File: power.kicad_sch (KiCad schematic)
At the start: 37 parts, among them J1 JST_PH_2.0mm_1x02, Q1 DMG2305UX-13, Q2 FS8205A, Q3 DMG2305UX-13, Q4 AO3400A, Q5 AO3400A, U1 DW01A, U2 LP5907MFX-3.3/NOPB, U3 TP4056, U4 LP5907MFX-3.3/NOPB, U5 SD6210A

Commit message: New components added, schematic being completed
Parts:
- added C38, C42, C54: 10u, sldrnrd:C_1206, symbol sldrnrd:Capacitor/C1206_10u
- added C40, C44: 100n, sldrnrd:C_0603, symbol sldrnrd:Capacitor/C0603_100n
- added C45: 1u, sldrnrd:C_0805, symbol sldrnrd:Capacitor/C0805_1u
- added R33: 68k, sldrnrd:R_0603, symbol sldrnrd:Resistor/R0603_68k
- added R35: 180k, sldrnrd:R_0603, symbol sldrnrd:Resistor/R0603_180k
- added U17: LM27761DSGR, sldrnrd:WSON-8-2x2-EP, symbol sldrnrd:Power/ChargePump/LM27761DSGR
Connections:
- net 5V0: now also C38.1, C40.1, U17.1 (VIN), U17.6 (EN)
- net GND: now also C38.2, C40.2, C42.2, C44.2, C54.2, R33.2, U17.2 (GND), U17.9 (EP)
- new net: R33.1, R35.2, U17.5 (VFB)
- new net: C54.1, U17.3 (CPOUT)
- new net: C45.1, U17.8 (C1+)
- new net: C45.2, U17.7 (C1-)
- new net -4V5: C42.1, C44.1, R35.1, U17.4 (VOUT)
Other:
- note added: "LM27761 Voltage Inverter"
- moved on the sheet: C1, C10, C11, C12, C14, C15, C2, C4, C6, C8, C9, Q3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

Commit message: Board layout without errors
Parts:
- renumbered C11 to C10, C7 to C11, C14 to C13, C15 to C14, C45 to C15, C54 to C16, C38 to C17, C40 to C18, C13 to C19, C42 to C20, C44 to C21, C4 to C3, C6 to C4, C3 to C5, C8 to C6, C9 to C7, C10 to C8, C5 to C9, Q3 to Q2, Q2 to Q3, R8 to R10, R9 to R11, R35 to R8, R33 to R9, U2 to U1, U1 to U2, U4 to U3, U3 to U4, U17 to U6

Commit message: Unavailable parts replaced, rotation issues fixed in library, except for U7
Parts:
- Q3: footprint sldrnrd:TSSOP-8 -> sldrnrd:SOT-23-6; symbol sldrnrd:Transistor/MosfetN/FS8205A -> sldrnrd:Transistor/MosfetN/FS8205A_TechPublic; LCSC C14212 -> C2830320; Manufacturer Fortune Semicon -> TECH PUBLIC
- R2: value 2k -> 1k; symbol sldrnrd:Resistor/R0603_2k -> sldrnrd:Resistor/R0603_1k; LCSC C22975 -> C21190; MPN 0603WAF2001T5E -> 0603WAF1001T5E
- R3: value 1k -> 470R; symbol sldrnrd:Resistor/R0603_1k -> sldrnrd:Resistor/R0603_470R; LCSC C21190 -> C23179; MPN 0603WAF1001T5E -> 0603WAF4700T5E
- U2: symbol sldrnrd:Power/BatteryManagement/DW01A -> sldrnrd:Power/BatteryManagement/DW01A_PUOLOP; LCSC C85680 -> C351410; Manufacturer Fortune Semicon -> PUOLOP
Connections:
- net BAT-: now also Q3.1 (S1); no longer Q3.2 (S1), Q3.3 (S1)
- net GND: now also Q3.3 (S2); no longer Q3.6 (S2), Q3.7 (S2)
- net at Q3.4 (G2): now also U2.3 (OC); no longer U2.1 (OD)
- net at Q3.5 (D): no longer U2.3 (OC)
- new net: Q3.6 (G1), U2.1 (OD)
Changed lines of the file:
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@@
 		(color 0 0 0 0)
 	)
-	(junction
-		(at 236.22 92.71)
-		(diameter 0)
-		(color 0 0 0 0)
-	)
 	(no_connect
 		(at 363.22 82.55)
@@
 	(wire
 		(pts
-			(xy 201.93 92.71) (xy 199.39 92.71)
-		)
-		(stroke
-			(width 0)
-			(type default)
-		)
-	)
-	(wire
-		(pts
 			(xy 344.17 184.15) (xy 334.01 184.15)
 		)
@@
 	(wire
 		(pts
-			(xy 219.71 92.71) (xy 236.22 92.71)
-		)
-		(stroke
-			(width 0)
-			(type default)
-		)
-	)
-	(wire
-		(pts
 			(xy 251.46 170.18) (xy 251.46 187.96)
 		)
@@
 	(wire
 		(pts
-			(xy 236.22 92.71) (xy 236.22 105.41)
-		)
-		(stroke
-			(width 0)
-			(type default)
-		)
-	)
-	(wire
-		(pts
 			(xy 190.5 187.96) (xy 205.74 187.96)
 		)
@@
 	(wire
 		(pts
+			(xy 203.2 95.25) (xy 203.2 105.41)
+		)
+		(stroke
+			(width 0)
+			(type default)
+		)
+	)
+	(wire
+		(pts
 			(xy 508 92.71) (xy 496.57 92.71)
 		)
@@
 	(wire
 		(pts
-			(xy 199.39 90.17) (xy 199.39 92.71)
-		)
-		(stroke
-			(width 0)
-			(type default)
-		)
-	)
-	(wire
-		(pts
 			(xy 186.69 63.5) (xy 186.69 77.47)
 		)
@@
 	(wire
 		(pts
-			(xy 193.04 95.25) (xy 201.93 95.25)
+			(xy 204.47 95.25) (xy 203.2 95.25)
 		)
 		(stroke
@@
 	(wire
 		(pts
+			(xy 219.71 83.82) (xy 193.04 83.82)
+		)
+		(stroke
+			(width 0)
+			(type default)
+		)
+	)
+	(wire
+		(pts
 			(xy 363.22 77.47) (xy 386.08 77.47)
 		)
@@
 	(wire
 		(pts
-			(xy 374.65 184.15) (xy 383.54 184.15)
+			(xy 217.17 95.25) (xy 226.06 95.25)
 		)
 		(stroke
@@
 	(wire
 		(pts
-			(xy 226.06 80.01) (xy 226.06 95.25)
+			(xy 374.65 184.15) (xy 383.54 184.15)
 		)
 		(stroke
@@
 	(wire
 		(pts
-			(xy 236.22 90.17) (xy 236.22 92.71)
+			(xy 226.06 80.01) (xy 226.06 95.25)
 		)
 		(stroke
@@
 	(wire
 		(pts
-			(xy 219.71 95.25) (xy 226.06 95.25)
-		)
-		(stroke
-			(width 0)
-			(type default)
-		)
-	)
-	(wire
-		(pts
 			(xy 318.77 168.91) (xy 318.77 181.61)
 		)
@@
 	(wire
 		(pts
-			(xy 193.04 60.96) (xy 193.04 95.25)
+			(xy 193.04 60.96) (xy 193.04 83.82)
 		)
 		(stroke
@@
 	(wire
 		(pts
+			(xy 219.71 90.17) (xy 219.71 83.82)
+		)
+		(stroke
+			(width 0)
+			(type default)
+		)
+	)
+	(wire
+		(pts
 			(xy 190.5 187.96) (xy 190.5 199.39)
 		)
@@
 	(wire
 		(pts
+			(xy 217.17 90.17) (xy 219.71 90.17)
+		)
+		(stroke
+			(width 0)
+			(type default)
+		)
+	)
+	(wire
+		(pts
 			(xy 81.28 205.74) (xy 81.28 220.98)
 		)
@@
 	(wire
 		(pts
-			(xy 199.39 90.17) (xy 201.93 90.17)
+			(xy 199.39 90.17) (xy 204.47 90.17)
 		)
 		(stroke
@@
 	(wire
 		(pts
-			(xy 219.71 90.17) (xy 236.22 90.17)
-		)
-		(stroke
-			(width 0)
-			(type default)
-		)
-	)
-	(wire
-		(pts
 			(xy 190.5 204.47) (xy 190.5 219.71)
 		)
@@
 	)
 	(symbol
-		(lib_id "sldrnrd:Transistor/MosfetN/FS8205A")
-		(at 210.82 91.44 0)
+		(lib_id "sldrnrd:Transistor/MosfetN/FS8205A_TechPublic")
+		(at 210.82 92.71 270)
 		(unit 1)
 		(body_style 1)
@@
 		(dnp no)
 		(property "Reference" "Q3"
-			(at 210.82 83.82 0)
+			(at 218.44 92.71 0)
 			(show_name no)
 			(do_not_autoplace no)
@@
 		)
 		(property "Value" "FS8205A"
-			(at 210.82 99.06 0)
+			(at 201.93 92.71 0)
 			(show_name no)
 			(do_not_autoplace no)
@@
 			)
 		)
-		(property "Footprint" "sldrnrd:TSSOP-8"
-			(at 210.82 102.87 0)
+		(property "Footprint" "sldrnrd:SOT-23-6"
+			(at 199.39 92.71 0)
 			(hide yes)
 			(show_name no)
@@
 			)
 		)
-		(property "Datasheet" "${SLDRNRD_LIB}/datasheets/Transistor/MosfetN/FS8205A.pdf"
-			(at 210.82 105.41 0)
+		(property "Datasheet" "${SLDRNRD_LIB}/datasheets/Transistor/MosfetN/FS8205A_TechPublic.pdf"
+			(at 196.85 92.71 0)
 			(hide yes)
 			(show_name no)
@@
 		)
 		(property "Description" ""
-			(at 210.82 91.44 0)
+			(at 210.82 92.71 0)
 			(hide yes)
 			(show_name no)
@@
 			)
 		)
-		(property "Manufacturer" "Fortune Semicon"
-			(at 210.82 107.95 0)
+		(property "Manufacturer" "TECH PUBLIC"
+			(at 194.31 92.71 0)
 			(hide yes)
 			(show_name no)
@@
 		)
 		(property "MPN" "FS8205A"
-			(at 210.82 110.49 0)
+			(at 191.77 92.71 0)
 			(hide yes)
 			(show_name no)
@@
 			)
 		)
-		(property "LCSC" "C14212"
-			(at 210.82 113.03 0)
+		(property "LCSC" "C2830320"
+			(at 189.23 92.71 0)
 			(hide yes)
 			(show_name no)
@@
 		(pin "6"
 		)
-		(pin "7"
-		)
 		(pin "2"
 		)
-		(pin "8"
-		)
 		(pin "3"
 		)
@@
 	)
 	(symbol
-		(lib_id "sldrnrd:Resistor/R0603_1k")
+		(lib_id "sldrnrd:Resistor/R0603_470R")
 		(at 234.95 57.15 180)
 		(unit 1)
@@
 			)
 		)
-		(property "Value" "1k"
-			(at 239.014 57.15 90)
+		(property "Value" "470R"
+			(at 236.982 57.15 90)
 			(show_name no)
 			(do_not_autoplace no)
@@
 			)
 		)
-		(property "Description" "1k Resistor, 0603, 1%, 75V, 100mW"
+		(property "Description" "470R Resistor, 0603, 1%, 75V, 100mW"
 			(at 234.95 57.15 0)
 			(hide yes)
@@
 			)
 		)
-		(property "MPN" "0603WAF1001T5E"
+		(property "MPN" "0603WAF4700T5E"
 			(at 234.95 57.15 0)
 			(hide yes)
@@
 			)
 		)
-		(property "LCSC" "C21190"
+		(property "LCSC" "C23179"
 			(at 234.95 57.15 0)
 			(hide yes)
@@
 		(in_pos_files yes)
 		(dnp no)
-		(fields_autoplaced yes)
 		(property "Reference" "C5"
 			(at 237.49 67.3099 90)
@@
 		)
 		(property "Value" "100n"
-			(at 237.49 69.8499 90)
+			(at 239.268 68.58 90)
 			(show_name no)
 			(do_not_autoplace no)
@@
 	)
 	(symbol
-		(lib_id "sldrnrd:Resistor/R0603_2k")
+		(lib_id "sldrnrd:Resistor/R0603_1k")
 		(at 186.69 81.28 0)
 		(unit 1)
@@
 		(fields_autoplaced yes)
 		(property "Reference" "R2"
-			(at 189.23 80.0099 90)
+			(at 189.23 80.0099 0)
 			(show_name no)
 			(do_not_autoplace no)
@@
 					(size 1.27 1.27)
 				)
+				(justify left)
 			)
 		)
-		(property "Value" "2k"
-			(at 189.23 82.5499 90)
+		(property "Value" "1k"
+			(at 189.23 82.5499 0)
 			(show_name no)
 			(do_not_autoplace no)
@@
 					(size 1.27 1.27)
 				)
+				(justify left)
 			)
 		)
@@
 			)
 		)
-		(property "Description" "2k Resistor, 0603, 1%, 75V, 100mW"
+		(property "Description" "1k Resistor, 0603, 1%, 75V, 100mW"
 			(at 186.69 81.28 0)
 			(hide yes)
@@
 			)
 		)
-		(property "MPN" "0603WAF2001T5E"
+		(property "MPN" "0603WAF1001T5E"
 			(at 186.69 81.28 0)
 			(hide yes)
@@
 			)
 		)
-		(property "LCSC" "C22975"
+		(property "LCSC" "C21190"
 			(at 186.69 81.28 0)
 			(hide yes)
@@
 	(symbol
 		(lib_id "sldrnrd:PowerFlag/GND")
-		(at 236.22 105.41 0)
+		(at 203.2 105.41 0)
 		(unit 1)
 		(body_style 1)
@@
 		(fields_autoplaced yes)
 		(property "Reference" "#PWR015"
-			(at 236.22 111.76 0)
+			(at 203.2 111.76 0)
 			(hide yes)
 			(show_name no)
@@
 		)
 		(property "Value" "GND"
-			(at 236.22 110.49 0)
+			(at 203.2 110.49 0)
 			(show_name no)
 			(do_not_autoplace no)
@@
 		)
 		(property "Footprint" ""
-			(at 236.22 105.41 0)
+			(at 203.2 105.41 0)
 			(hide yes)
 			(show_name no)
@@
 		)
 		(property "Datasheet" "~"
-			(at 236.22 105.41 0)
+			(at 203.2 105.41 0)
 			(hide yes)
 			(show_name no)
@@
 		)
 		(property "Description" "Power symbol creates a global label with name \"GND\", ground"
-			(at 236.22 105.41 0)
+			(at 203.2 105.41 0)
 			(hide yes)
 			(show_name no)
@@
 	)
 	(symbol
-		(lib_id "sldrnrd:Power/BatteryManagement/DW01A")
+		(lib_id "sldrnrd:Power/BatteryManagement/DW01A_PUOLOP")
 		(at 210.82 63.5 0)
 		(unit 1)
@@
 			)
 		)
-		(property "Datasheet" "${SLDRNRD_LIB}/datasheets/Power/BatteryManagement/DW01A.pdf"
+		(property "Datasheet" "${SLDRNRD_LIB}/datasheets/Power/BatteryManagement/DW01A_PUOLOP.pdf"
 			(at 210.82 76.2 0)
 			(hide yes)
@@
 			)
 		)
-		(property "Description" ""
+		(property "Description" "1-Cell Li-ion Battery Protection IC, SOT-23-6"
 			(at 210.82 63.5 0)
 			(hide yes)
@@
 			)
 		)
-		(property "Manufacturer" "Fortune Semicon"
+		(property "Manufacturer" "PUOLOP"
 			(at 210.82 78.74 0)
 			(hide yes)
@@
 			)
 		)
-		(property "LCSC" "C85680"
+		(property "LCSC" "C351410"
 			(at 210.82 83.82 0)
 			(hide yes)

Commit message: Fix stock/pinout issues, re-export fabrication files, apply JLC rotation corrections
- Replace out-of-stock parts (D2/D3 LED, U5, U10) with in-stock JLCPCB
  alternatives; add D5-D12 protection diodes
- Fix U2/DW01A footprint rotation on PCB
- Re-export gerbers, drill files, and JLCSMT BOM/CPL from current design
- BOM/CPL: DS1 uses header connector LCSC number only (display bought
  separately), U13 (LM35) and mounting holes excluded as do-not-place
- CPL rotations for U7, U5, Q3, U2 corrected per known JLCPCB
  per-part orientation quirks (see sldrnrd_kicad_lib/JLC_ROTATION_OFFSETS.md)
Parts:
- D2: symbol sldrnrd:LED/LED_Green_0603 -> sldrnrd:LED/LED_Green_0603_NationStar; LCSC C72043 -> C87326; MPN 19-217/GHC-YR1S2/3T -> NCD0603G2; Manufacturer EVERLIGHT -> NationStar
- U5: value SD6210A -> HX4002-MFC; symbol sldrnrd:Power/ChargePump/SD6210A -> sldrnrd:Power/ChargePump/HX4002-MFC; LCSC C250809 -> C172354; MPN SD6210A -> HX4002-MFC; Manufacturer SHOUDING -> HEXIN
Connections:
- net 3V3: now also D1.2 (A), D2.2 (A); no longer D1.1 (A), D2.1 (A)
- net at R6.1: now also D1.1 (K); no longer D1.2 (K)
- net at R7.1: now also D2.1 (K); no longer D2.2 (K)
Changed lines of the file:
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@@
 	(wire
 		(pts
-			(xy 420.37 62.23) (xy 420.37 64.77)
-		)
-		(stroke
-			(width 0)
-			(type default)
-		)
-	)
-	(wire
-		(pts
 			(xy 251.46 170.18) (xy 251.46 187.96)
 		)
@@
 	(wire
 		(pts
-			(xy 411.48 50.8) (xy 411.48 54.61)
-		)
-		(stroke
-			(width 0)
-			(type default)
-		)
-	)
-	(wire
-		(pts
 			(xy 369.57 186.69) (xy 388.62 186.69)
 		)
@@
 	(wire
 		(pts
-			(xy 488.95 187.96) (xy 494.03 187.96)
+			(xy 420.37 62.23) (xy 420.37 64.77)
 		)
 		(stroke
@@
 	(wire
 		(pts
-			(xy 327.66 181.61) (xy 327.66 194.31)
+			(xy 488.95 187.96) (xy 494.03 187.96)
 		)
 		(stroke
@@
 	(wire
 		(pts
-			(xy 388.62 186.69) (xy 388.62 190.5)
+			(xy 327.66 181.61) (xy 327.66 194.31)
 		)
 		(stroke
@@
 	(wire
 		(pts
-			(xy 198.12 63.5) (xy 186.69 63.5)
+			(xy 388.62 186.69) (xy 388.62 190.5)
 		)
 		(stroke
@@
 	(wire
 		(pts
-			(xy 386.08 62.23) (xy 386.08 77.47)
+			(xy 198.12 63.5) (xy 186.69 63.5)
 		)
 		(stroke
@@
 	(wire
 		(pts
-			(xy 234.95 49.53) (xy 234.95 53.34)
+			(xy 386.08 62.23) (xy 386.08 77.47)
 		)
 		(stroke
@@
 	(wire
 		(pts
-			(xy 186.69 63.5) (xy 186.69 77.47)
+			(xy 234.95 49.53) (xy 234.95 53.34)
 		)
 		(stroke
@@
 	(wire
 		(pts
-			(xy 180.34 193.04) (xy 180.34 170.18)
+			(xy 186.69 63.5) (xy 186.69 77.47)
 		)
 		(stroke
@@
 	(wire
 		(pts
-			(xy 420.37 50.8) (xy 420.37 54.61)
+			(xy 180.34 193.04) (xy 180.34 170.18)
 		)
 		(stroke
@@
 	(wire
 		(pts
-			(xy 411.48 62.23) (xy 411.48 64.77)
+			(xy 64.77 106.68) (xy 64.77 73.66)
 		)
 		(stroke
@@
 	(wire
 		(pts
-			(xy 64.77 106.68) (xy 64.77 73.66)
+			(xy 519.43 203.2) (xy 519.43 204.47)
 		)
 		(stroke
@@
 	(wire
 		(pts
-			(xy 519.43 203.2) (xy 519.43 204.47)
+			(xy 327.66 199.39) (xy 327.66 207.01)
 		)
 		(stroke
@@
 	(wire
 		(pts
-			(xy 327.66 199.39) (xy 327.66 207.01)
+			(xy 307.34 80.01) (xy 307.34 106.68)
 		)
 		(stroke
@@
 	(wire
 		(pts
-			(xy 307.34 80.01) (xy 307.34 106.68)
+			(xy 193.04 60.96) (xy 198.12 60.96)
 		)
 		(stroke
@@
 	(wire
 		(pts
-			(xy 193.04 60.96) (xy 198.12 60.96)
+			(xy 386.08 50.8) (xy 386.08 54.61)
 		)
 		(stroke
@@
 	(wire
 		(pts
-			(xy 386.08 50.8) (xy 386.08 54.61)
+			(xy 420.37 50.8) (xy 420.37 54.61)
 		)
 		(stroke
@@
 	(wire
 		(pts
+			(xy 411.48 62.23) (xy 411.48 64.77)
+		)
+		(stroke
+			(width 0)
+			(type default)
+		)
+	)
+	(wire
+		(pts
 			(xy 81.28 189.23) (xy 81.28 200.66)
 		)
@@
 	(wire
 		(pts
+			(xy 411.48 50.8) (xy 411.48 54.61)
+		)
+		(stroke
+			(width 0)
+			(type default)
+		)
+	)
+	(wire
+		(pts
 			(xy 448.31 187.96) (xy 453.39 187.96)
 		)
@@
 		)
 		(property "Value" "68k"
-			(at 438.15 199.3899 0)
+			(at 438.15 199.3899 90)
 			(show_name no)
 			(do_not_autoplace no)
@@
 					(size 1.27 1.27)
 				)
-				(justify left)
 			)
 		)
@@
 	)
 	(symbol
-		(lib_id "sldrnrd:LED/LED_Green_0603")
+		(lib_id "sldrnrd:LED/LED_Green_0603_NationStar")
 		(at 420.37 58.42 90)
 		(unit 1)
@@
 		)
 		(property "Value" "LED_Green_0603"
-			(at 420.37 54.61 90)
+			(at 420.37 60.96 90)
 			(show_name no)
 			(do_not_autoplace no)
@@
 			)
 		)
-		(property "Description" ""
+		(property "Description" "Green LED, 0603"
 			(at 420.37 58.42 0)
 			(hide yes)
@@
 			)
 		)
-		(property "Manufacturer" "EVERLIGHT"
+		(property "Manufacturer" "NationStar"
 			(at 420.37 58.42 0)
 			(hide yes)
@@
 			)
 		)
-		(property "MPN" "19-217/GHC-YR1S2/3T"
+		(property "MPN" "NCD0603G2"
 			(at 420.37 58.42 0)
 			(hide yes)
@@
 			)
 		)
-		(property "LCSC" "C72043"
+		(property "LCSC" "C87326"
 			(at 420.37 58.42 0)
 			(hide yes)
@@
 		)
 		(property "Value" "180k"
-			(at 438.15 186.6899 0)
+			(at 438.15 186.6899 90)
 			(show_name no)
 			(do_not_autoplace no)
@@
 					(size 1.27 1.27)
 				)
-				(justify left)
 			)
 		)
@@
 		)
 		(property "Value" "1k"
-			(at 189.23 82.5499 0)
+			(at 189.23 82.5499 90)
 			(show_name no)
 			(do_not_autoplace no)
@@
 					(size 1.27 1.27)
 				)
-				(justify left)
 			)
 		)
@@
 	)
 	(symbol
-		(lib_id "sldrnrd:Power/ChargePump/SD6210A")
+		(lib_id "sldrnrd:Power/ChargePump/HX4002-MFC")
 		(at 356.87 184.15 0)
 		(unit 1)
@@
 			)
 		)
-		(property "Value" "SD6210A"
+		(property "Value" "HX4002-MFC"
 			(at 356.87 191.77 0)
 			(show_name no)
@@
 			)
 		)
-		(property "Datasheet" "${SLDRNRD_LIB}/datasheets/Power/ChargePump/SD6210A.pdf"
+		(property "Datasheet" "${SLDRNRD_LIB}/datasheets/Power/ChargePump/HX4002-MFC.pdf"
 			(at 356.87 196.85 0)
 			(hide yes)
@@
 			)
 		)
-		(property "Description" ""
+		(property "Description" "Charge Pump 5V 250mA, SOT-23-6"
 			(at 356.87 184.15 0)
 			(hide yes)
@@
 			)
 		)
-		(property "Manufacturer" "SHOUDING"
+		(property "Manufacturer" "HEXIN"
 			(at 356.87 199.39 0)
 			(hide yes)
@@
 			)
 		)
-		(property "MPN" "SD6210A"
+		(property "MPN" "HX4002-MFC"
 			(at 356.87 201.93 0)
 			(hide yes)
@@
 			)
 		)
-		(property "LCSC" "C250809"
+		(property "LCSC" "C172354"
 			(at 356.87 204.47 0)
 			(hide yes)

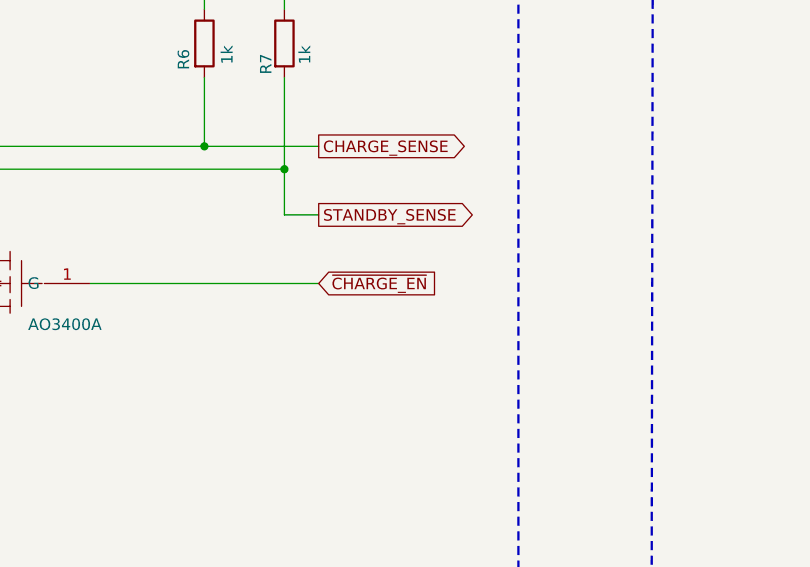
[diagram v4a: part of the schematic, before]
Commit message: Pinout description added, STM configuration added, netlist exported
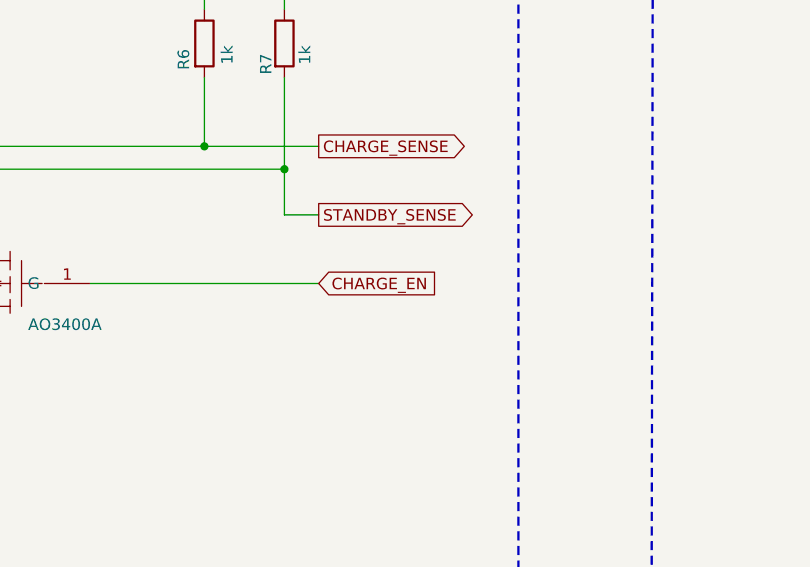
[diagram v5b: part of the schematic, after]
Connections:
- net ~{CHARGE_EN} renamed CHARGE_EN
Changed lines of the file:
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@@
 		)
 	)
-	(global_label "~{CHARGE_EN}"
+	(global_label "CHARGE_EN"
 		(shape input)
 		(at 424.18 95.25 0)

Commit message: Schematic checks, some smaller corrections, debug UART pinout corrected on programming header
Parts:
- added C69, C70: 10u, sldrnrd:C_1206, symbol sldrnrd:Capacitor/C1206_10u
- added R57: 100k, sldrnrd:R_0603, symbol sldrnrd:Resistor/R0603_100k
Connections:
- net 3V3: now also R57.1
- net 3V3_STANDBY: now also C69.1, C70.1
- net GND: now also C69.2, C70.2, R57.2
- net CHARGE_EN renamed ~{CHARGE_EN}
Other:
- moved on the sheet: C1, C15, C16, C17, C18, C2, C20, C21, R8, R9, U1, U6

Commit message: Further checks. Capacitors unified to basic parts
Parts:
- C11, C13, C16, C17, C20, C3, C69, C7, C70, C8, C9: footprint sldrnrd:C_1206 -> sldrnrd:C_0805; symbol sldrnrd:Capacitor/C1206_10u -> sldrnrd:Capacitor/C0805_10u; Dielectric X7R -> X5R; LCSC C70462 -> C440198; MPN CC1206KKX7R8BB106 -> GRM21BR61H106KE43L; Manufacturer Yageo -> Murata; Voltage 25V -> 50V
- C14: Dielectric X7R -> X5R; LCSC C126589 -> C377773; MPN GCM21BR71C225KA64L -> CL21A225KBQNNNE; Manufacturer Murata -> Samsung Electro-Mechanics; Voltage 16V -> 50V

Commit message: LEVELMETER Rev A as ordered
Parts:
- D2: value LED_Green_0603 -> LED_Red_0603; symbol sldrnrd:LED/LED_Green_0603_NationStar -> sldrnrd:LED/LED_Red_0603; LCSC C87326 -> C2286; MPN NCD0603G2 -> KT-0603R; Manufacturer NationStar -> KENTO
- Q1, Q2: value DMG2305UX-13 -> AO3401A; symbol sldrnrd:Transistor/MosfetP/DMG2305UX-13 -> sldrnrd:Transistor/MosfetP/AO3401A; LCSC C144153 -> C15127; MPN DMG2305UX-13 -> AO3401A; Manufacturer Diodes Inc. -> Alpha & Omega Semiconductor
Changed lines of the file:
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@@
 	)
 	(symbol
-		(lib_id "sldrnrd:LED/LED_Green_0603_NationStar")
+		(lib_id "sldrnrd:LED/LED_Red_0603")
 		(at 420.37 58.42 90)
 		(unit 1)
@@
 		(dnp no)
 		(property "Reference" "D2"
-			(at 423.164 58.42 90)
+			(at 420.37 55.88 90)
 			(show_name no)
 			(do_not_autoplace no)
@@
 			)
 		)
-		(property "Value" "LED_Green_0603"
+		(property "Value" "LED_Red_0603"
 			(at 420.37 60.96 90)
 			(show_name no)
@@
 			)
 		)
-		(property "Manufacturer" "NationStar"
+		(property "Manufacturer" "KENTO"
 			(at 420.37 58.42 0)
 			(hide yes)
@@
 			)
 		)
-		(property "MPN" "NCD0603G2"
+		(property "MPN" "KT-0603R"
 			(at 420.37 58.42 0)
 			(hide yes)
@@
 			)
 		)
-		(property "LCSC" "C87326"
+		(property "LCSC" "C2286"
 			(at 420.37 58.42 0)
 			(hide yes)
@@
 	)
 	(symbol
-		(lib_id "sldrnrd:Transistor/MosfetP/DMG2305UX-13")
+		(lib_id "sldrnrd:Transistor/MosfetP/AO3401A")
 		(at 78.74 78.74 90)
 		(unit 1)
@@
 		(dnp no)
 		(property "Reference" "Q1"
-			(at 74.168 77.47 0)
+			(at 73.914 76.454 0)
 			(show_name no)
 			(do_not_autoplace no)
@@
 			)
 		)
-		(property "Value" "DMG2305UX-13"
-			(at 84.328 70.866 0)
+		(property "Value" "AO3401A"
+			(at 83.82 78.994 0)
 			(show_name no)
 			(do_not_autoplace no)
@@
 			)
 		)
-		(property "Datasheet" "${SLDRNRD_LIB}/datasheets/Transistor/MosfetP/DMG2305UX.pdf"
+		(property "Datasheet" "${SLDRNRD_LIB}/datasheets/Transistor/MosfetP/AO3401A.pdf"
 			(at 99.06 78.74 0)
 			(hide yes)
@@
 			)
 		)
-		(property "Manufacturer" "Diodes Inc."
+		(property "Manufacturer" "Alpha & Omega Semiconductor"
 			(at 101.6 78.74 0)
 			(hide yes)
@@
 			)
 		)
-		(property "MPN" "DMG2305UX-13"
+		(property "MPN" "AO3401A"
 			(at 104.14 78.74 0)
 			(hide yes)
@@
 			)
 		)
-		(property "LCSC" "C144153"
+		(property "LCSC" "C15127"
 			(at 106.68 78.74 0)
 			(hide yes)
@@
 	)
 	(symbol
-		(lib_id "sldrnrd:Transistor/MosfetP/DMG2305UX-13")
+		(lib_id "sldrnrd:Transistor/MosfetP/AO3401A")
 		(at 101.6 194.31 270)
 		(mirror x)
@@
 		(dnp no)
 		(property "Reference" "Q2"
-			(at 106.172 193.04 0)
+			(at 116.84 194.31 0)
 			(show_name no)
 			(do_not_autoplace no)
@@
 			)
 		)
-		(property "Value" "DMG2305UX-13"
-			(at 96.012 186.436 0)
+		(property "Value" "AO3401A"
+			(at 86.36 194.31 0)
 			(show_name no)
 			(do_not_autoplace no)
@@
 			)
 		)
-		(property "Datasheet" "${SLDRNRD_LIB}/datasheets/Transistor/MosfetP/DMG2305UX.pdf"
+		(property "Datasheet" "${SLDRNRD_LIB}/datasheets/Transistor/MosfetP/AO3401A.pdf"
 			(at 81.28 194.31 0)
 			(hide yes)
@@
 			)
 		)
-		(property "Manufacturer" "Diodes Inc."
+		(property "Manufacturer" "Alpha & Omega Semiconductor"
 			(at 78.74 194.31 0)
 			(hide yes)
@@
 			)
 		)
-		(property "MPN" "DMG2305UX-13"
+		(property "MPN" "AO3401A"
 			(at 76.2 194.31 0)
 			(hide yes)
@@
 			)
 		)
-		(property "LCSC" "C144153"
+		(property "LCSC" "C15127"
 			(at 73.66 194.31 0)
 			(hide yes)
@@
 		)
 	)
-	(embedded_fonts no)
 )
